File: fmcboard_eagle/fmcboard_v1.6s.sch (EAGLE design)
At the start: 300 parts, among them IC1 OPA699ID, IC10 LM358, IC11 7805DT, IC12 SN74AUC2G66DCTR, IC13 SN74AUC2G66DCTR, IC14 SN74AUC2G66DCTR, IC15 SN74AUC2G66DCTR, IC16 DAC7578SPWR, IC17 SN74AUC2G66DCTR, IC18 SN74AUC2G66DCTR, IC19 SN74AUC2G66DCTR, IC2 DAC7578SPWR, IC20 SN74AUC2G66DCTR, IC21 74AUP2GU04GW, IC22 74AUP2GU04GW, IC23 74AUP2GU04GW, IC24 74AUP2GU04GW, IC25 MC7905ACD2TR4G, IC26 AMS1117-1.8, IC27 LM358, IC28 SN74AUC2G66DCTR, IC29 LM337KVURG3, IC3 LTC6229IMS8E#TRPBF, IC30 SN74AUC2G66DCTR, IC31 SN74AUC2G66DCTR, IC32 SN74AUC2G66DCTR, IC33 LTC6229IMS8E#TRPBF, IC34 74AUP2GU04GW, IC35 74AUP2GU04GW, IC36 TPS5430DDAR, IC37 TPS5430DDAR, IC4 OPA695IDR, IC5 LTC6229IMS8E#TRPBF, IC6 OPA695IDR, IC7 OPA699ID, IC8 LM358, IC9 LM358, J1 8pin, J12 4p-2.54, J13 4p-2.54, J2 ASP-134604-01, J3 2p-2.54, J4 4p-2.54, J5 4p-2.54, J8 4p-2.54, J9 2p-2.54

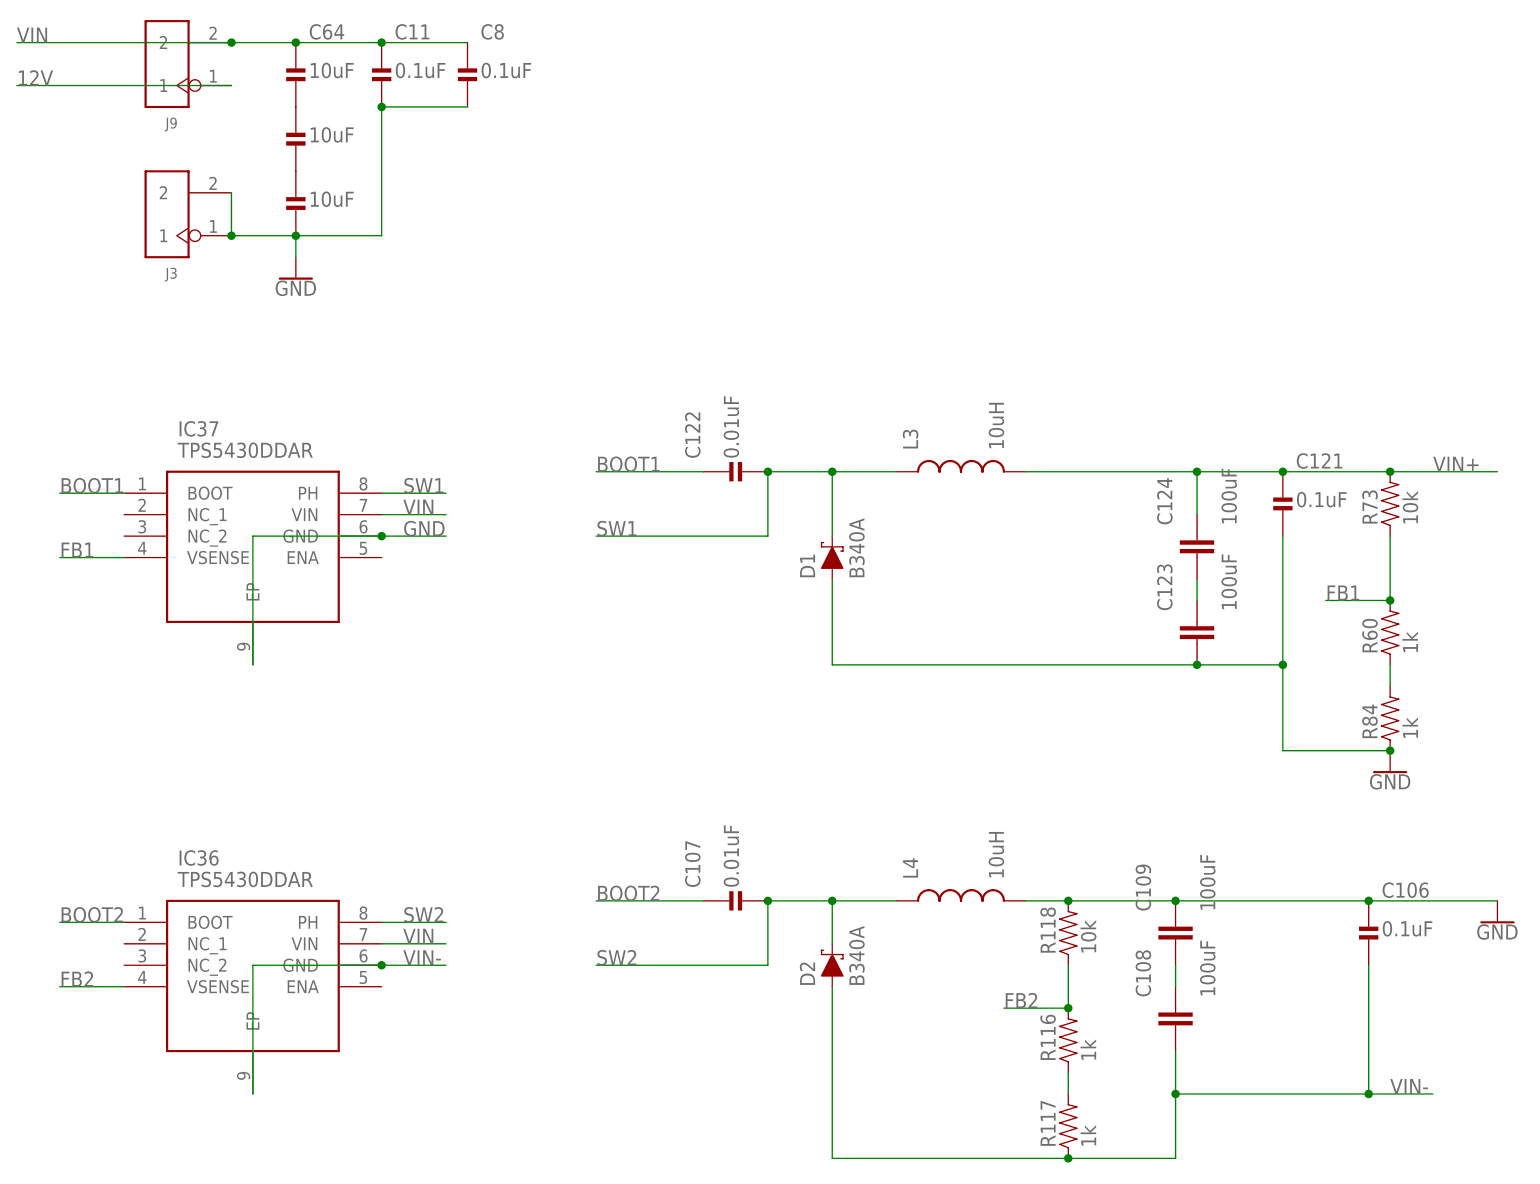
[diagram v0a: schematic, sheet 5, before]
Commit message: remove sdain sclin c26 c27 holes clean up +-7 V schematic
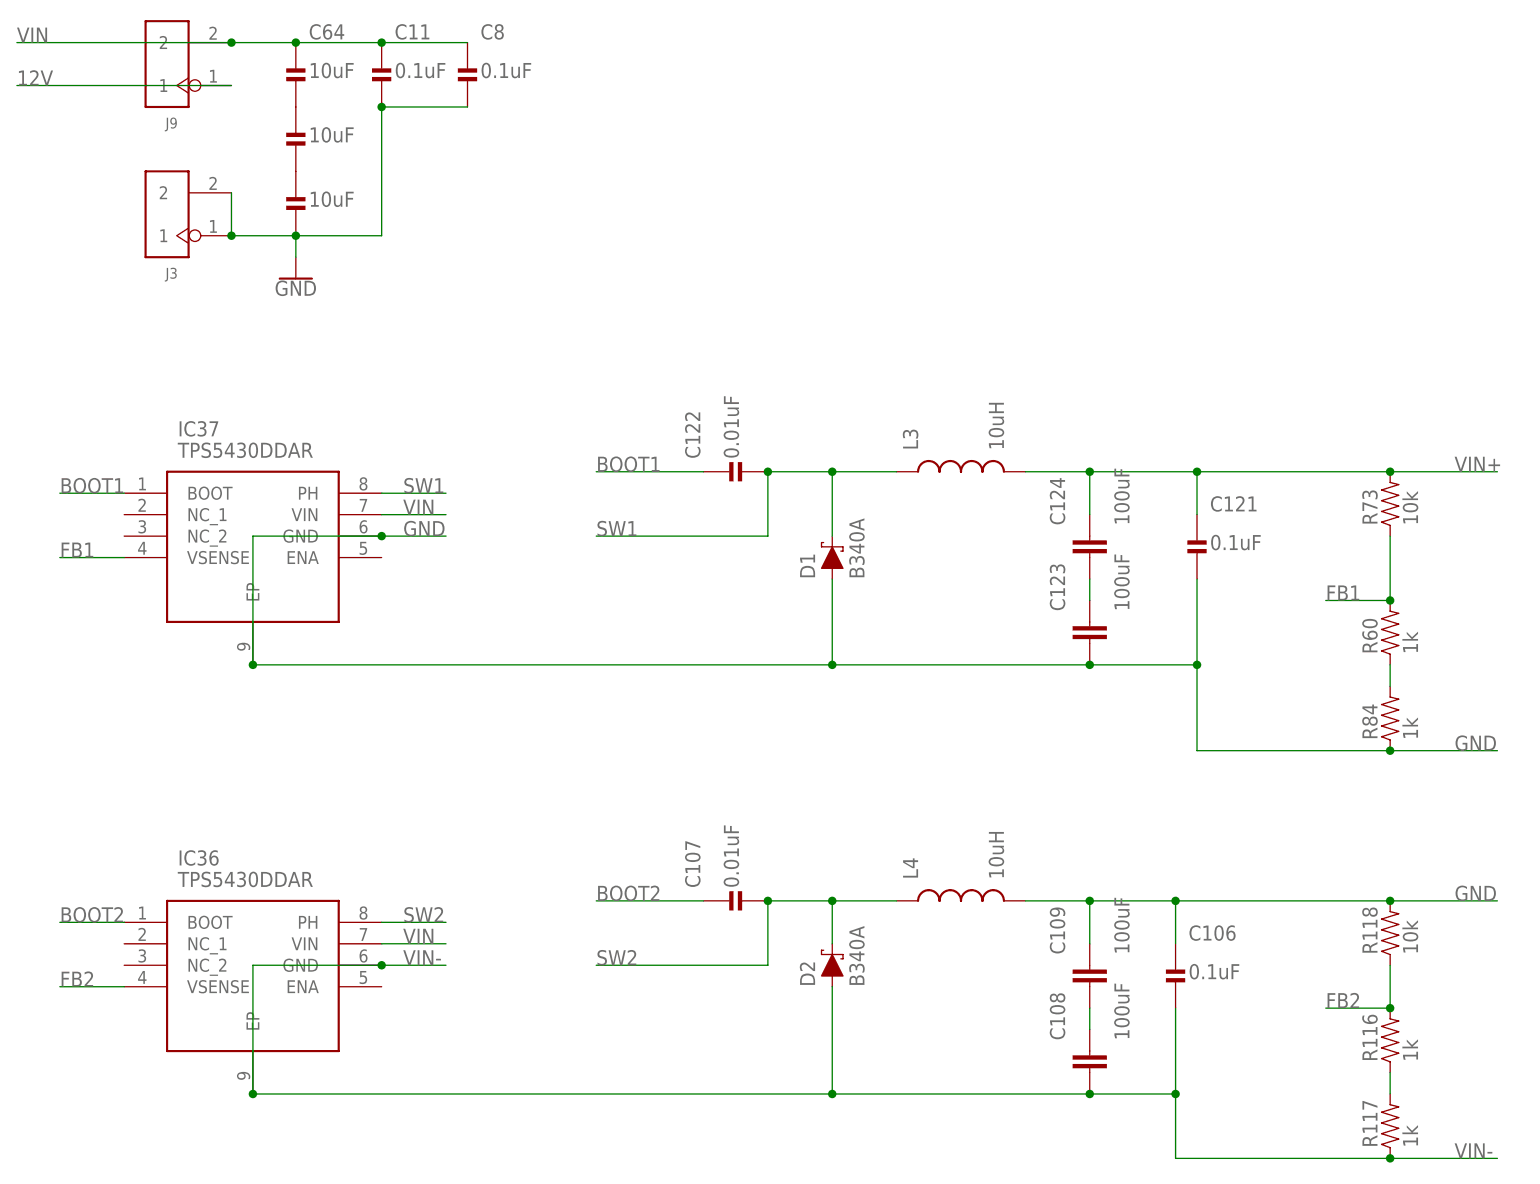
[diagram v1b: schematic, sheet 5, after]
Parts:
- removed J4: 4p-2.54, Seeed-Connector:DIP-BLACK-FEMALE-HEADER-VERT(4P-2.54)
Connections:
- net C26: no longer J4.P$3
- net C27: no longer J4.P$4
- net SCLIN: no longer J4.P$2
- net SDAIN: no longer J4.P$1
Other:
- moved on the sheet: C106, C108, C109, C121, C123, C124, R116, R117, R118

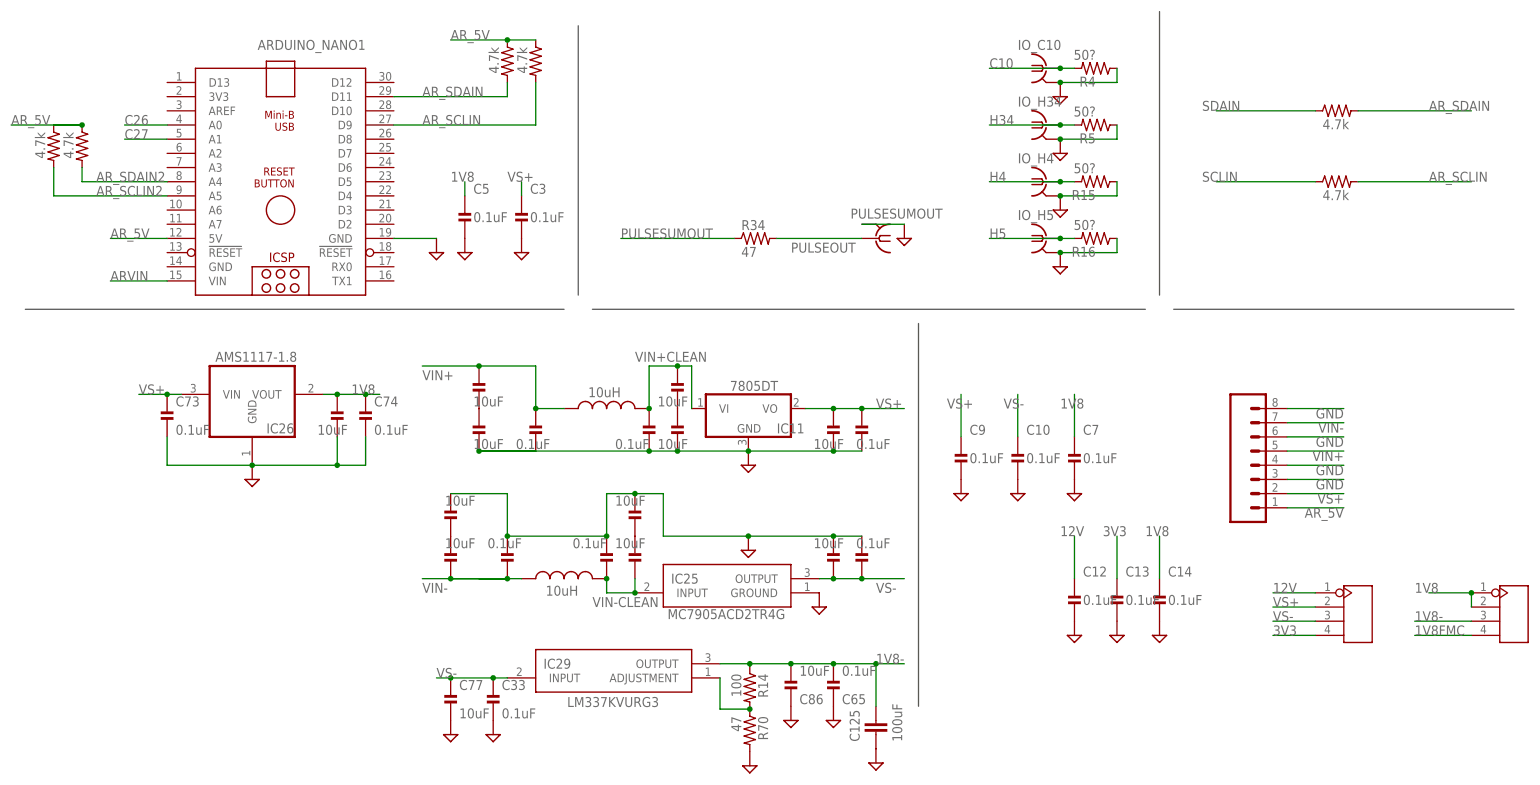
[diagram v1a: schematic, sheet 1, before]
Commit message: 0805 10uF
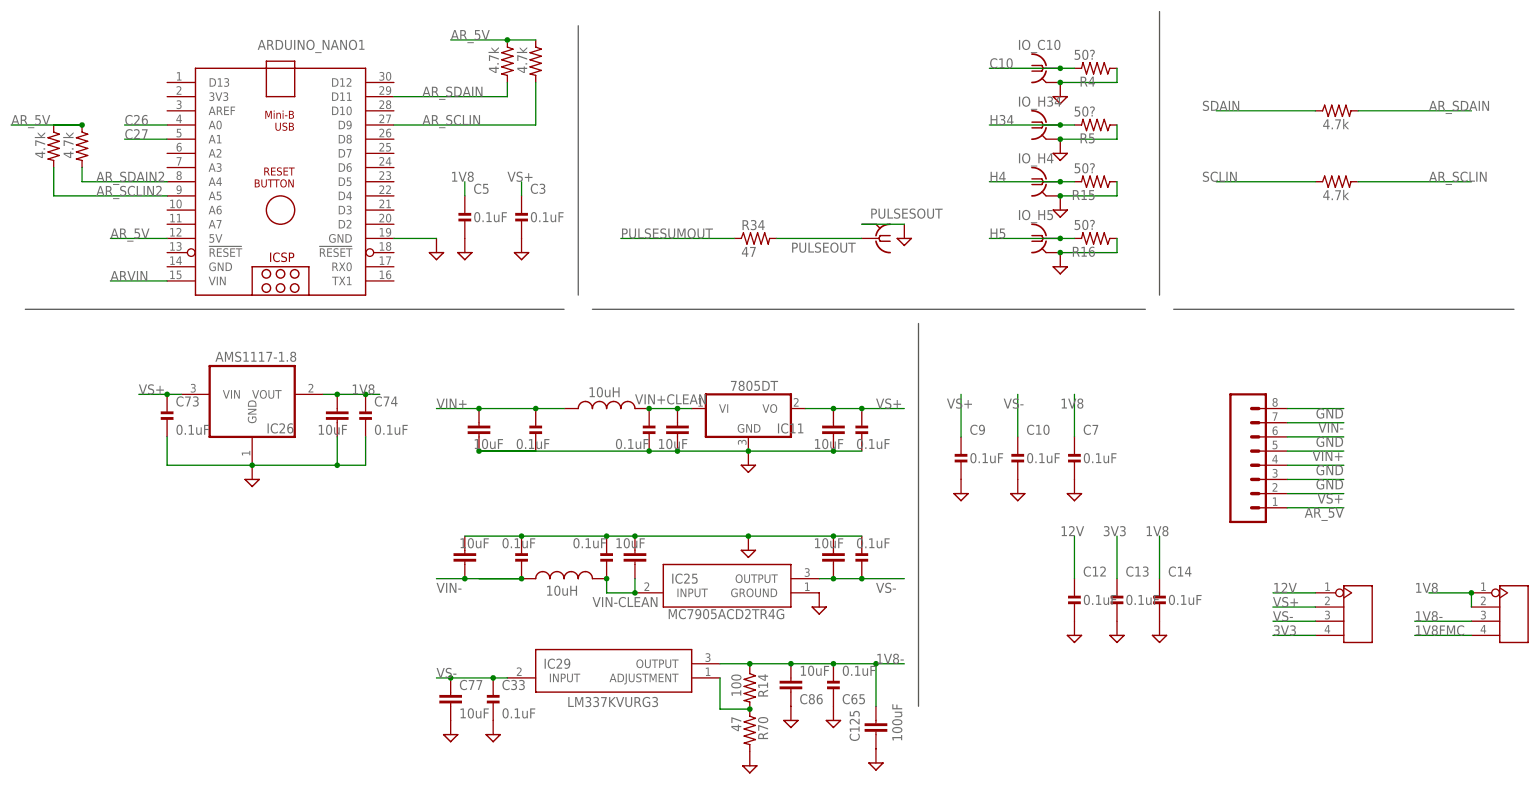
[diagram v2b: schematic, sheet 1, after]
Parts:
- removed C118, C119, C2, C40, C80: 10uF, passives:CAPACITOR0402_CAP
- C1, C110, C111, C120, C34, C38, C39, C41, C64, C77, C86: device passives:CAPACITOR0402_CAP -> rcl:C-EUC0805
- renumbered PULSESUMOUT to PULSESOUT
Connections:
- removed net N$35: J13.P$2, R71.1
- removed net N$38: C1.1, C118.2
- removed net N$39: C119.2, C41.1
- removed net N$52: C120.2, C80.1
- removed net N$58: C110.1, C2.2
- removed net N$59: C111.1, C40.2
- new net N$57: J13.P$4, R71.1
- net GND: now also C111.1, C120.2, C41.1, J13.P$2, J13.P$3; no longer C119.1, C40.1, C80.2
- net VIN+: now also C1.1; no longer C118.1
- net VIN+CLEAN: now also C110.1; no longer C2.1
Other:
- moved on the sheet: R71
